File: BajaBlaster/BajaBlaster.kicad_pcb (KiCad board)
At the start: 4 copper layers, 59.2 x 45.8 mm, 48 parts, among them J201 Conn_01x02_Pin, J501 Conn_01x06_Pin, J502 INTERBOARD, J503 Conn_01x04_Pin, SW301 SW_Push, SW302 SW_Push, U201 AP2112K-3.3, U202 TPS562200, U301 ESP32-WROOM-32, U302 MPU-6050, U501 TCAN330

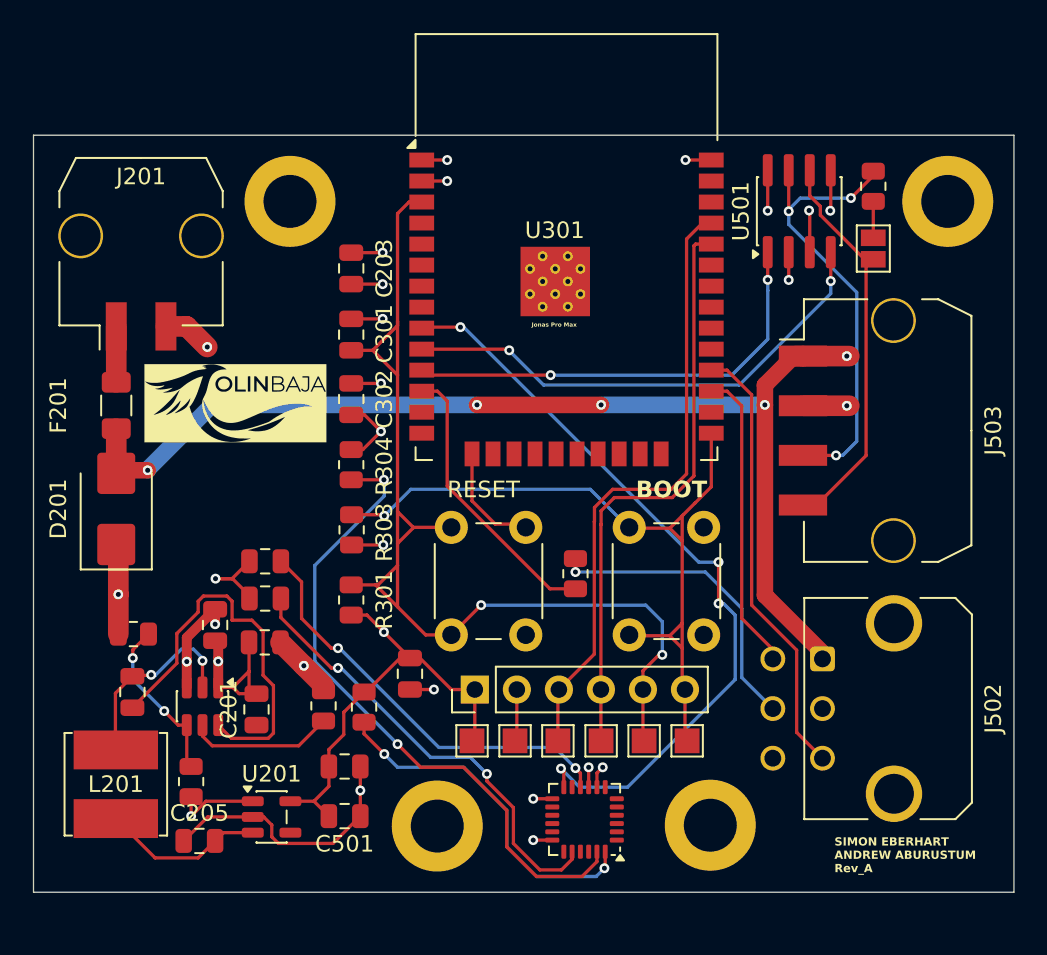
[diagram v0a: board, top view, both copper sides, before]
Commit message: erc passed no errors 30 warnings
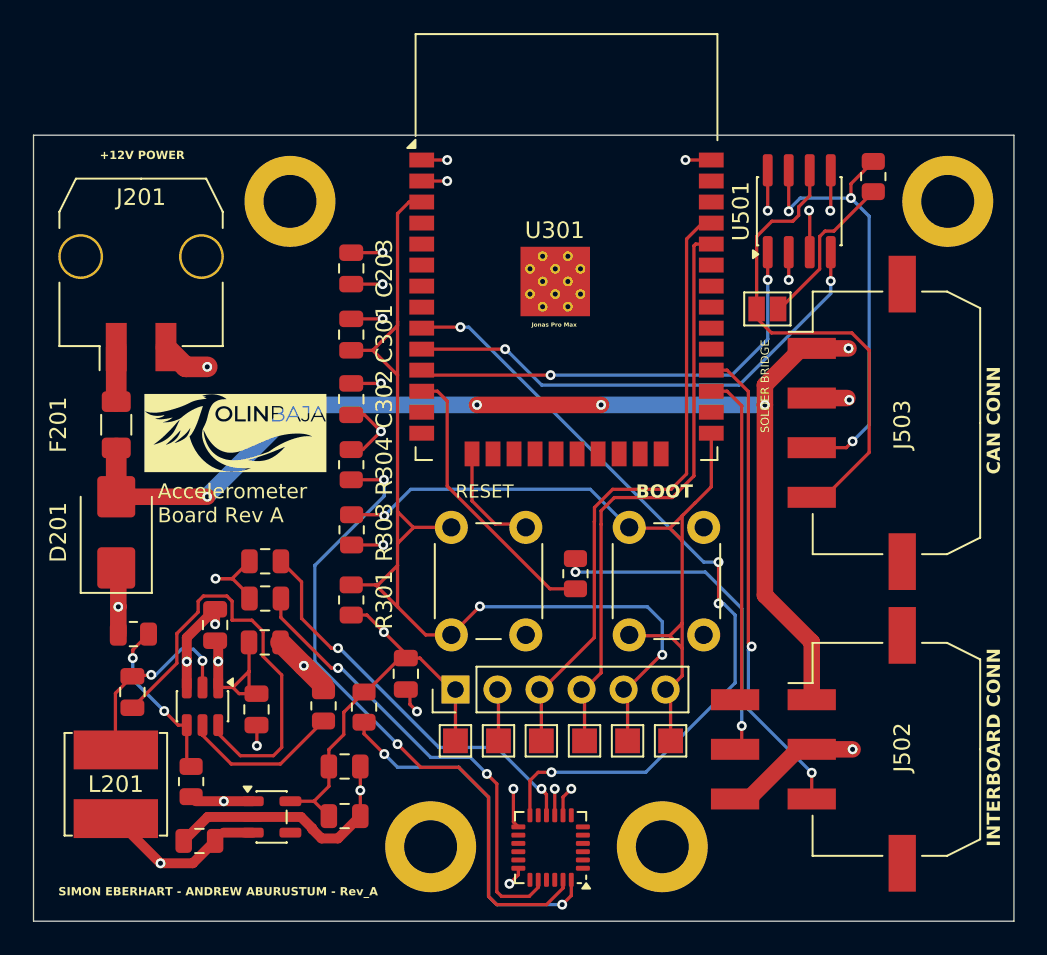
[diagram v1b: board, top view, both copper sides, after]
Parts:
- added G***: LOGO, Logos:BajaLogoLarge, B.Cu at (54.6, 97.9)
- J502: footprint Connector_Molex:Molex_Micro-Fit_3.0_43045-0621_2x03-1MP_P3.00mm_Horizontal -> Connector_Molex:Molex_Micro-Fit_3.0_43045-0610_2x03-1MP_P3.00mm_Horizontal
- J503: footprint Connector_Molex:Molex_Micro-Fit_3.0_43650-0410_1x04-1MP_P3.00mm_Horizontal -> Connector_Molex:Molex_Micro-Fit_3.0_43650-0412_1x04-1MP_P3.00mm_Horizontal
- moved JP501 7.37 mm to (69.3, 85.5), turned to 180 degrees
- moved J502 6.22 mm to (69.7, 112.1)
- moved REF** 3.18 mm to (63.0, 118.0)
- moved U302 2.66 mm to (56.2, 118.0)
- moved G*** 1.80 mm to (37.2, 93.0)
- moved D201 1.42 mm to (30.0, 99.0)
- moved REF** 1.31 mm to (49.0, 118.0)
- moved J201 1.25 mm to (31.5, 82.7)
- moved J501 1.17 mm to (50.5, 108.5)
- moved F201 1.17 mm to (30.0, 92.5)
- moved REF** 1.00 mm to (50.5, 111.6)
- moved REF** 1.00 mm to (58.3, 111.6)
- moved REF** 1.00 mm to (55.7, 111.6)
- moved REF** 1.00 mm to (53.1, 111.6)
- moved REF** 1.00 mm to (60.9, 111.6)
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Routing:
- net Net-(JP501-A): track 2.20 -> 9.83 mm
- net /COMMS/CANL: track 24.4 -> 30.6 mm
- net GND: track 71.9 -> 77.2 mm, vias 17 -> 18
- net +12V: track 77.8 -> 81.2 mm
- net /COMMS/INTERBOARD_TX: track 26.8 -> 29.3 mm, vias 0 -> 2
- net Net-(U202-VBST): track 23.9 -> 26.3 mm
- net /MCU/INT: track 46.5 -> 48.7 mm
- net /COMMS/SYNC: track 18.8 -> 20.6 mm, vias 1 -> 2
- net /COMMS/INTERBOARD_RX: track 18.3 -> 20.1 mm
- net Net-(U302-REGOUT): track 25.7 -> 24.5 mm
- net /POWER/VREG_EN: track 8.84 -> 9.72 mm
- net Net-(U302-SDA): track 21.3 -> 22.2 mm
- net Net-(U302-CPOUT): track 27.3 -> 28.2 mm
- net Net-(U302-SCL): track 39.4 -> 40.2 mm
- net +5V: track 15.2 -> 15.3 mm, vias 1 -> 3
- added copper zone on In2.Cu, net +5V
- removed copper zone on In2.Cu, net (none)
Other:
- board size 59.2 x 45.8 mm -> 59.2 x 47.5 mm
- board text added: "+12V POWER"
- board text added: "Accelerometer Board Rev A"
- board text added: "CAN CONN"
- board text added: "INTERBOARD CONN"
- board text added: "SIMON EBERHART - ANDREW ABURUSTUM - Rev_A"
- board text added: "SOLDER BRIDGE"
- board text removed: "SIMON EBERHART ANDREW ABURUSTUM Rev_A"

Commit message: fixed wiring per isa and aryans recs
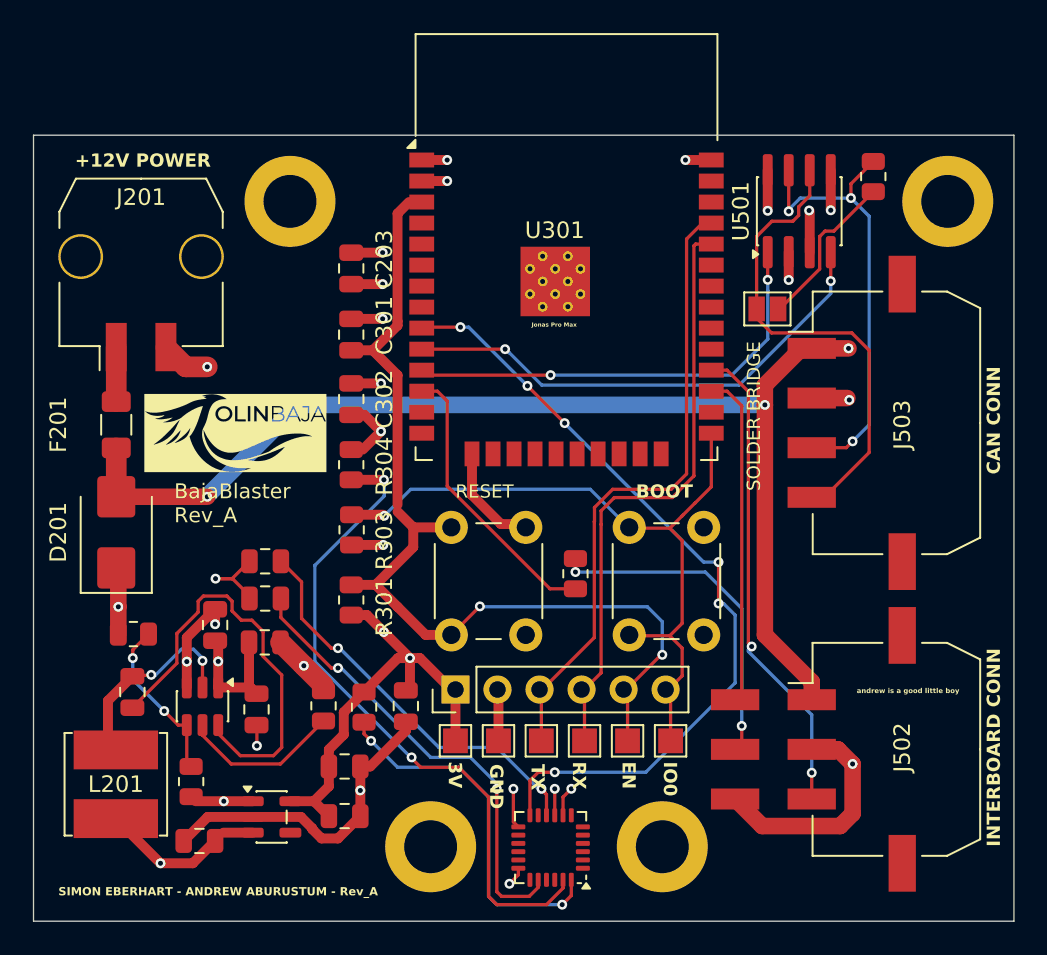
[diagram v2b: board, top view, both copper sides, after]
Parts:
- moved C303 1.95 mm to (47.5, 109.5)
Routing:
- net GND: track 77.2 -> 86.1 mm, vias 18 -> 17
- net /COMMS/ESP32_EN: track 67.7 -> 60.0 mm
- net /COMMS/IO0: track 47.3 -> 44.3 mm
- net +3V3: track 42.1 -> 44.1 mm, vias 8 -> 9
- net +12V: vias 8 -> 6
- net /MCU/INT: vias 4 -> 6
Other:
- board text added: "3V"
- board text added: "BajaBlaster Rev_A"
- board text added: "EN"
- board text added: "GND"
- board text added: "IO0"
- board text added: "RX"
- board text added: "TX"
- board text added: "andrew is a good little boy"
- board text removed: "Accelerometer Board Rev A"

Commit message: added power led indicator, double checked everything. passed erc
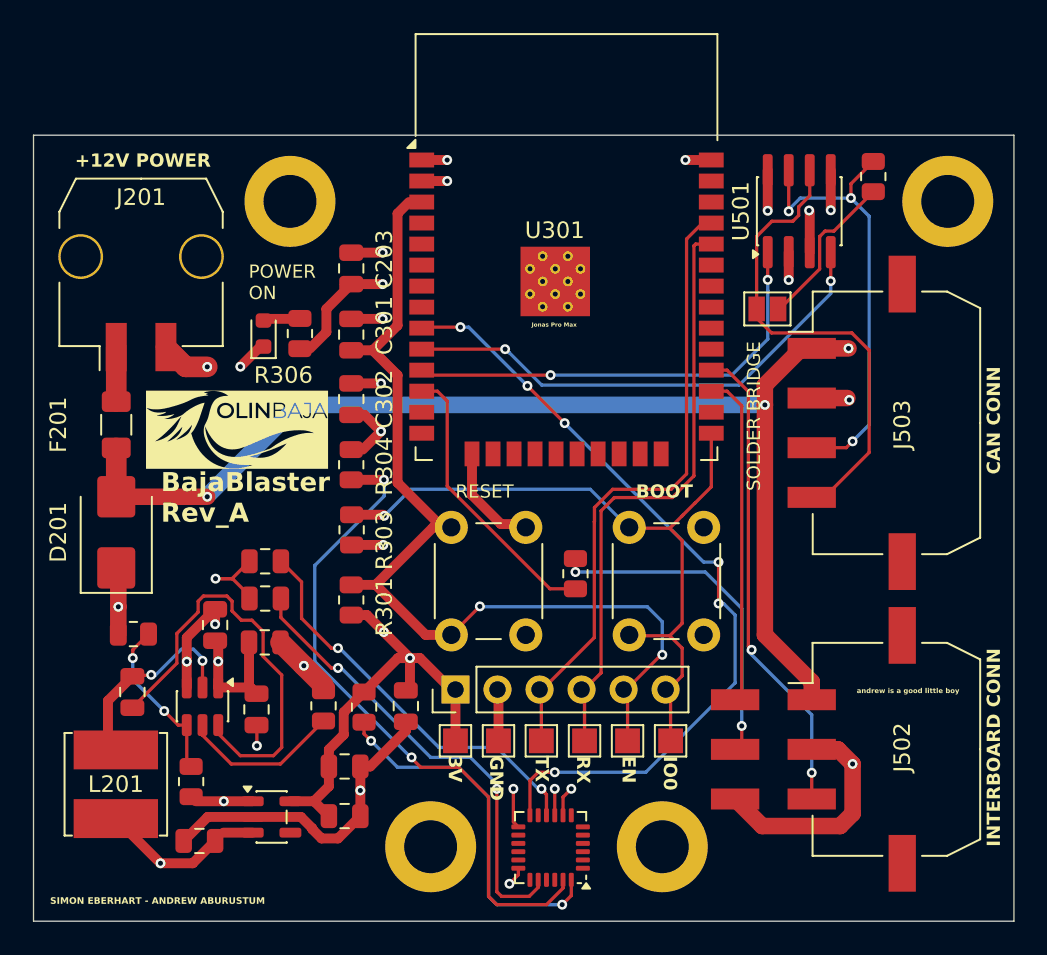
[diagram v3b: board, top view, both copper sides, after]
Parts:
- added D301: LED, LED_SMD:LED_0603_1608Metric, F.Cu at (38.9, 87.0)
- added R306: 1kOHM, Resistor_SMD:R_0805_2012Metric, F.Cu at (41.1, 87.0)
- R303: value 10kOhm -> 10kOHM
- moved G*** 0.22 mm to (37.3, 92.8)
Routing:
- net +3V3: track 44.1 -> 49.0 mm
- net Net-(D301-A): track 0.00 -> 2.25 mm
- net /COMMS/CANL: track 30.6 -> 29.3 mm
- net +12V: track 81.2 -> 80.2 mm
- net /COMMS/U0TXD: track 37.9 -> 37.1 mm
- net Net-(U202-SW): track 12.3 -> 11.5 mm
- net /COMMS/IO0: track 44.3 -> 43.8 mm
- net /COMMS/SYNC: track 20.6 -> 20.0 mm
- net /COMMS/INTERBOARD_RX: track 20.1 -> 19.6 mm
- net /COMMS/ESP32_EN: track 60.0 -> 59.4 mm
- net Net-(U202-VBST): track 26.0 -> 25.4 mm
- net /COMMS/CANH: track 28.1 -> 27.6 mm
- net GND: track 86.1 -> 85.6 mm, vias 17 -> 18
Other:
- board text added: "POWER ON"
- board text added: "SIMON EBERHART - ANDREW ABURUSTUM"
- board text removed: "SIMON EBERHART - ANDREW ABURUSTUM - Rev_A"
